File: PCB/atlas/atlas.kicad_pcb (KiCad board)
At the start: 2 copper layers, 260 x 92 mm, 78 parts, among them J1 TP_BRIDGE_IN_L, J2 TP_BRIDGE_OUT_L, J3 TP_BRIDGE_IN_R, J4 TP_OUTPUT_TO_XIAO_L, J5 TP_BRIDGE_OUT_R, J6 TP_OUTPUT_TO_XIAO_R, J7 BattConnect_R, J8 BattConnect_L, U1 xiao-ble, U2 xiao-ble

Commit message: updated xiao positioning and mirrored trackpoint pcb out connections for easier soldering
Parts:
- moved U1 2.85 mm to (28.5, 38.0)
- moved U2 2.83 mm to (271.5, 38.0)
- turned J4 to -90 degrees
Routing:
- net (no net): track 0.00 -> 43.3 mm
- net ROW2_R: track 211.9 -> 185.8 mm, vias 5 -> 3
- net TP_GND_R: track 82.5 -> 106.9 mm, vias 3 -> 5
- net TP_GND_L: track 76.2 -> 100.3 mm, vias 3 -> 1
- net TP_VCC_R: track 91.0 -> 113.4 mm
- net TP_DATA_L: track 73.7 -> 91.1 mm, vias 3 -> 2
- net ROW1_L: track 169.4 -> 156.0 mm, vias 1 -> 3
- net TP_RST_R: track 75.6 -> 85.4 mm, vias 3 -> 6
- net COL0_R: track 75.1 -> 67.3 mm, vias 0 -> 1
- net TP_CLK_L: track 78.6 -> 85.6 mm
- net TP_RST_L: track 73.3 -> 78.9 mm, vias 1 -> 3
- net ROW1_R: track 181.4 -> 175.9 mm, vias 1 -> 2
- net TP_CLK_R: track 72.7 -> 78.2 mm, vias 1 -> 2
- net COL3_R: track 143.8 -> 139.6 mm, vias 2 -> 1
- net VBAT_R: track 72.8 -> 76.6 mm, vias 2 -> 3
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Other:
- board size 260 x 92 mm -> 264 x 94 mm

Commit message: pcb edit
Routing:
- net VBAT_R: track 76.6 -> 73.1 mm
- net ROW2_R: vias 3 -> 2
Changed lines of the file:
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@@
-	)
-	(segment
-		(start 272.7 48.5)
-		(end 272.7 44.982944)
-		(width 0.2)
-		(layer "F.Cu")
-		(net 47)
 	)
 	(segment
@@
 		(net 67)
 	)
-	(via
-		(at 277.2 51.5)
-		(size 0.6)
-		(drill 0.3)
-		(layers "F.Cu" "B.Cu")
-		(net 67)
-	)

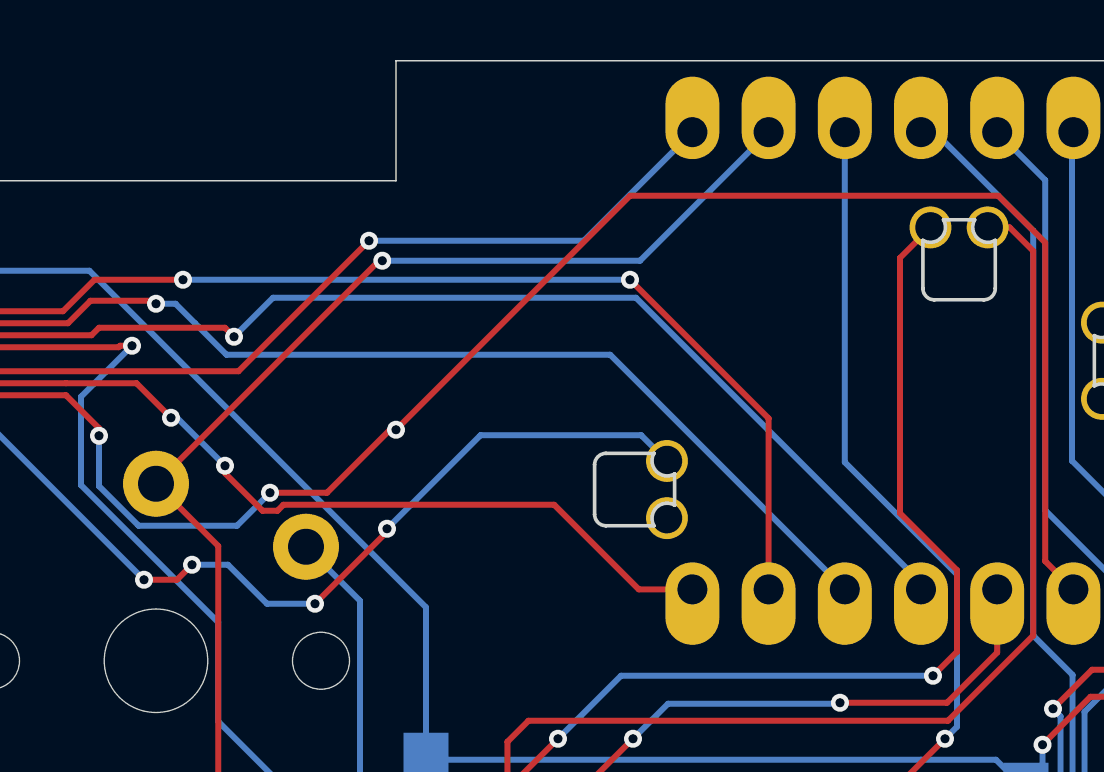
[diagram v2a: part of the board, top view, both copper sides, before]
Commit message: PCB fix, forgot a mounting hole
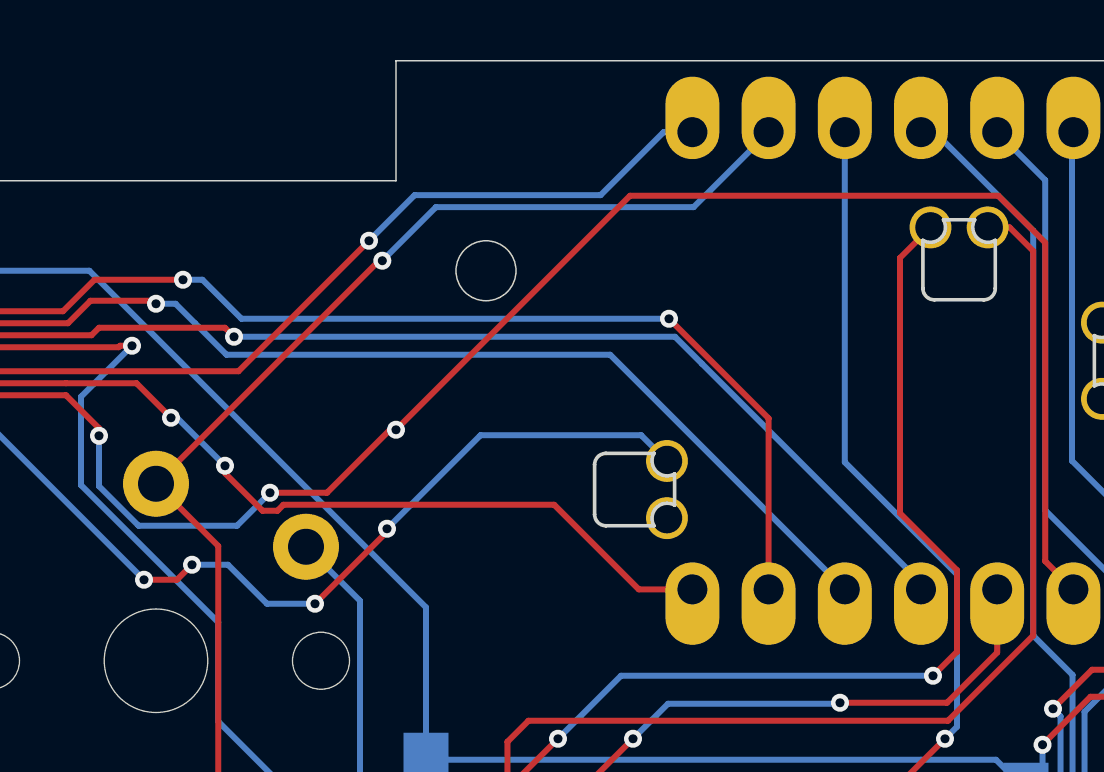
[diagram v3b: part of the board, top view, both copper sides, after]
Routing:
- net COL2_R: track 88.7 -> 87.6 mm
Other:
- outline, holes or cut-outs redrawn
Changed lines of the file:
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@@
 		(fp_arc
 			(start -4.0132 -2.475999)
-			(mid -4.095393 -1.872391)
+			(mid -4.095393 -1.872392)
 			(end -4.699 -1.7902)
 			(stroke
@@
 		(fp_arc
 			(start -4.0132 -2.475999)
-			(mid -4.095393 -1.872391)
+			(mid -4.095393 -1.872392)
 			(end -4.699 -1.7902)
 			(stroke
@@
 	)
 	(gr_circle
+		(center 257 35)
+		(end 258 35)
+		(stroke
+			(width 0.05)
+			(type solid)
+		)
+		(fill solid)
+		(layer "Edge.Cuts")
+	)
+	(gr_circle
 		(center 174 61)
 		(end 174 61.5)
@@
 	)
 	(segment
+		(start 262.92 30.38)
+		(end 263.88 30.38)
+		(width 0.2)
+		(layer "B.Cu")
+		(net 81)
+	)
+	(segment
+		(start 253.1 34)
+		(end 254.62 32.48)
+		(width 0.2)
+		(layer "B.Cu")
+		(net 81)
+	)
+	(segment
 		(start 231.499999 83.500001)
 		(end 233.1 81.9)
@@
 	)
 	(segment
-		(start 260.26 34)
-		(end 253.1 34)
+		(start 254.62 32.48)
+		(end 260.82 32.48)
 		(width 0.2)
 		(layer "B.Cu")
@@
 	)
 	(segment
-		(start 231.499999 85)
-		(end 231.499999 83.500001)
+		(start 260.82 32.48)
+		(end 262.92 30.38)
 		(width 0.2)
 		(layer "B.Cu")
@@
 	)
 	(segment
-		(start 263.88 30.38)
-		(end 260.26 34)
+		(start 231.499999 85)
+		(end 231.499999 83.500001)
 		(width 0.2)
 		(layer "B.Cu")
@@
 	)
 	(segment
-		(start 186 42)
-		(end 191.65 36.35)
+		(start 263.1 36.6)
+		(end 266.42 39.92)
 		(width 0.2)
 		(layer "F.Cu")
@@
 	)
 	(segment
-		(start 266.42 45.62)
-		(end 266.42 39.92)
+		(start 266.42 39.92)
+		(end 266.42 45.62)
+		(width 0.2)
+		(layer "F.Cu")
+		(net 86)
+	)
+	(segment
+		(start 186 42)
+		(end 191.65 36.35)
 		(width 0.2)
 		(layer "F.Cu")
@@
 	)
 	(segment
-		(start 266.42 39.92)
-		(end 261.8 35.3)
-		(width 0.2)
-		(layer "F.Cu")
-		(net 86)
-	)
-	(segment
 		(start 188.075 63.175)
 		(end 188.075 76.025)
@@
 	)
 	(via
-		(at 261.8 35.3)
+		(at 263.1 36.6)
 		(size 0.6)
 		(drill 0.3)
@@
 	)
 	(segment
-		(start 261.8 35.3)
-		(end 246.9 35.3)
+		(start 247.548529 35.3)
+		(end 248.848529 36.6)
+		(width 0.2)
+		(layer "B.Cu")
+		(net 86)
+	)
+	(segment
+		(start 248.848529 36.6)
+		(end 263.1 36.6)
+		(width 0.2)
+		(layer "B.Cu")
+		(net 86)
+	)
+	(segment
+		(start 246.9 35.3)
+		(end 247.548529 35.3)
 		(width 0.2)
 		(layer "B.Cu")
@@
 	)
 	(segment
-		(start 249.9 35.9)
-		(end 248.6 37.2)
+		(start 248.6 37.2)
+		(end 263.3 37.2)
 		(width 0.2)
 		(layer "B.Cu")
@@
 	)
 	(segment
-		(start 262 35.9)
-		(end 249.9 35.9)
+		(start 271.5 45.4)
+		(end 264.2 38.1)
 		(width 0.2)
 		(layer "B.Cu")
@@
 	)
 	(segment
-		(start 271.5 45.4)
-		(end 262 35.9)
+		(start 263.3 37.2)
+		(end 264.2 38.1)
 		(width 0.2)
 		(layer "B.Cu")
@@
 	)
 	(segment
-		(start 266.42 30.38)
-		(end 262.134358 34.665642)
+		(start 263.92 32.88)
+		(end 266.42 30.38)
+		(width 0.2)
+		(layer "B.Cu")
+		(net 89)
+	)
+	(segment
+		(start 253.543761 34.665642)
+		(end 255.329403 32.88)
 		(width 0.2)
 		(layer "B.Cu")
@@
 	)
 	(segment
-		(start 262.134358 34.665642)
-		(end 253.543761 34.665642)
+		(start 255.329403 32.88)
+		(end 263.92 32.88)
 		(width 0.2)
 		(layer "B.Cu")
